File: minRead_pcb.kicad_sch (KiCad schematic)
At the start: 119 parts, among them J1 USB_C_Receptacle, J2 FH34SRJ-24S-0.5SH_50_, J3 FH34SRJ-6S-0.5SH_50_, J5 Conn_01x02, J7 Micro_SD_Card, Q10 BSS138, Q11 BSS138, Q16 MMBT3906, Q17 MMBT3904, Q18 AO3419, Q4 [BSS138] AO3400A, Q5 AO3419, SW1 SW_Push, SW10 SW_Push, SW11 SW_Push, SW2 SW_Push, SW3 SW_Push, SW4 SW_Push, SW6 SW_Push, SW8 SW_Push, SW9 SW_Push, U1 TPD4E1U06DBVR, U11 AP3031KTR, U2 TPS2116DRL, U3 AP2112K-3.3, U4 ESP32-S3-WROOM-1, U6 TPD4E1U06DBVR, U7 MCP73832-2-OT

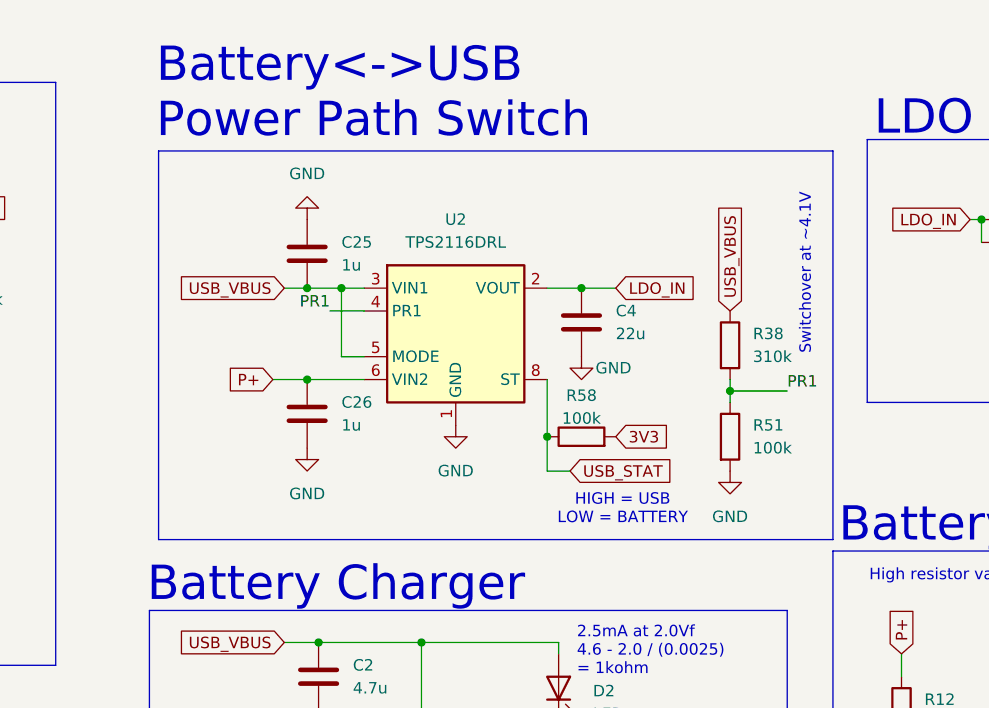
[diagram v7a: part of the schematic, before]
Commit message: simplify power path circuit design
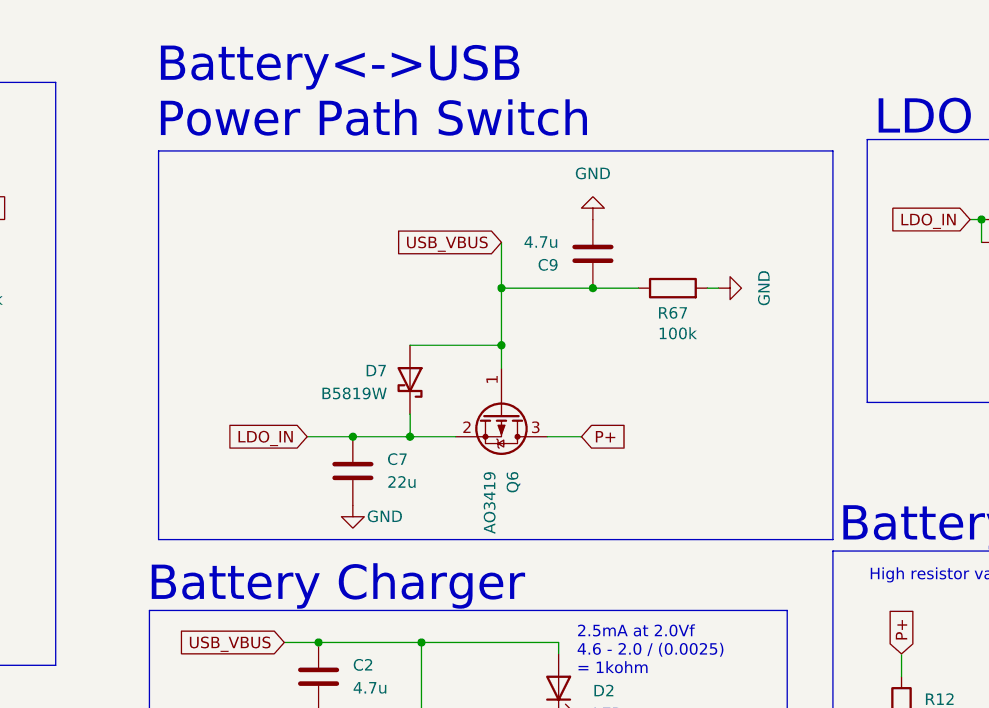
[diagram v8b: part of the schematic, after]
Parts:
- removed C25, C26: 1u, Capacitor_SMD:C_0805_2012Metric_Pad1.18x1.45mm_HandSolder, symbol Device:C
- removed C4: 22u, Capacitor_SMD:C_0805_2012Metric_Pad1.18x1.45mm_HandSolder, symbol Device:C
- removed R38: 310k, Resistor_SMD:R_0805_2012Metric_Pad1.20x1.40mm_HandSolder, symbol Device:R
- removed R51, R58: 100k, Resistor_SMD:R_0805_2012Metric_Pad1.20x1.40mm_HandSolder, symbol Device:R
- removed U2: TPS2116DRL, Package_TO_SOT_SMD:SOT-583-8, symbol Power_Management:TPS2116DRL
- added C7: 22u, Capacitor_SMD:C_0805_2012Metric_Pad1.18x1.45mm_HandSolder, symbol Device:C
- added C9: 4.7u, Capacitor_SMD:C_0805_2012Metric_Pad1.18x1.45mm_HandSolder, symbol Device:C
- added D7: B5819W, Diode_SMD:D_SOD-123, symbol Diode:MBR0530
- added Q6: AO3419, Package_TO_SOT_SMD:SOT-23_Handsoldering, symbol Transistor_FET:IRLML6402
- added R67: 100k, Resistor_SMD:R_0805_2012Metric_Pad1.20x1.40mm_HandSolder, symbol Device:R
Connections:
- net GND: now also C7.2, C9.2, R67.2
- net LDO_IN: now also C7.1, D7.1 (K), Q6.2 (S)
- net P+: now also Q6.3 (D)
- net USB_VBUS: now also C9.1, D7.2 (A), Q6.1 (G), R67.1
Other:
- note removed: "HIGH = USB LOW = BATTERY"
- note removed: "Switchover at ~4.1V"
